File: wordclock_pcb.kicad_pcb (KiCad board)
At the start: 2 copper layers, 97.5 x 78.2 mm, 45 parts, among them IC1 ATmega328P, J1 MYUSBCONN5, J2 Stecker 1, J3 Stecker 2, J4 Stecker 3, Q1 2N3904, Q2 2N3904, SW1 MYSWITCH2, SW2 MYSWITCH_reduced, SW3 MYSWITCH_reduced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

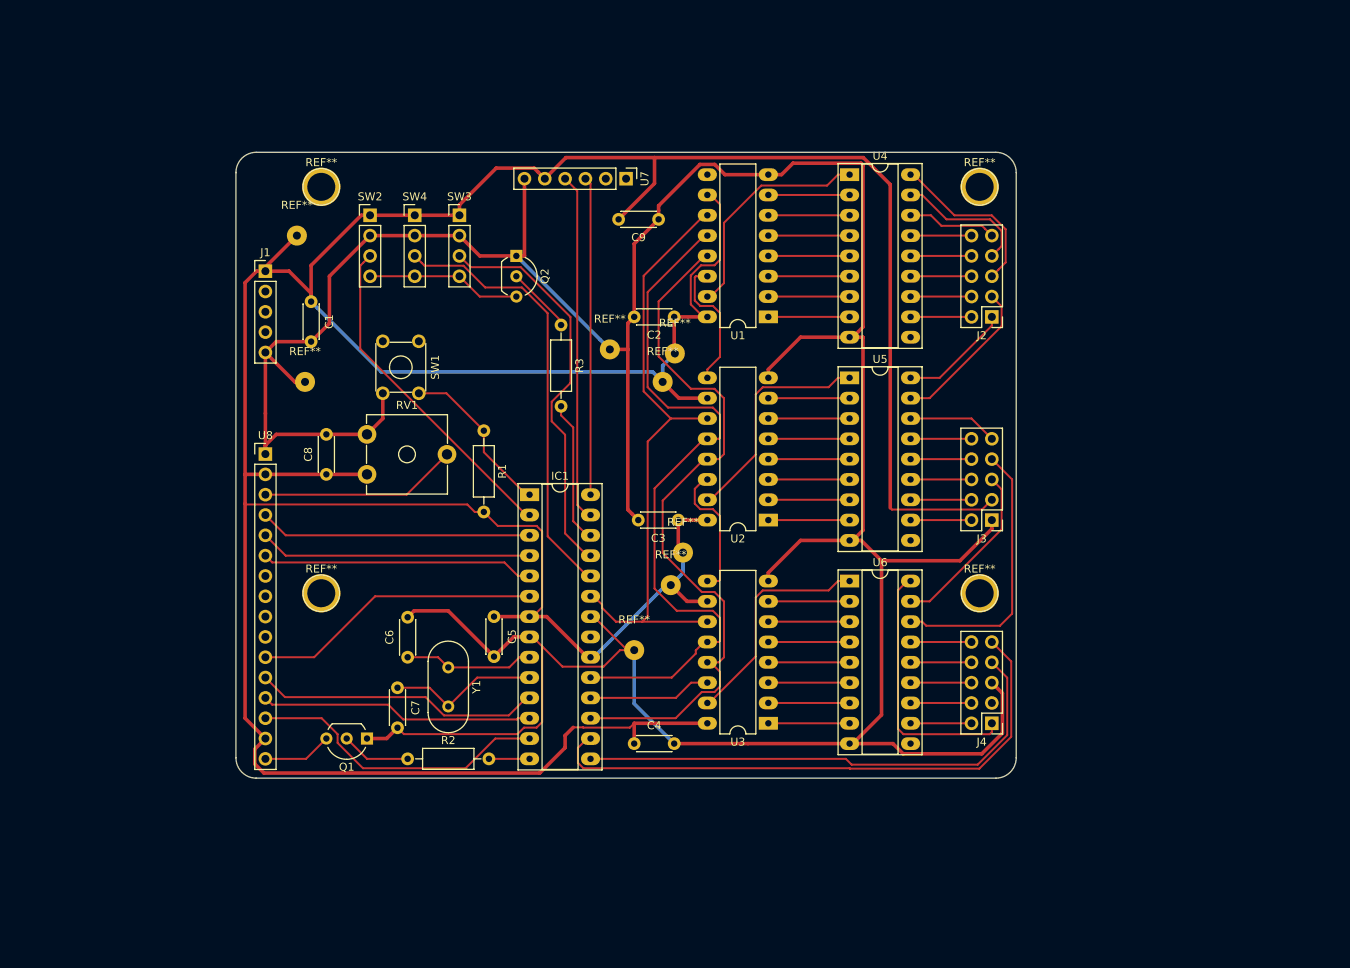
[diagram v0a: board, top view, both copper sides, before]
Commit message: Delete old pcb design and arrange footprints
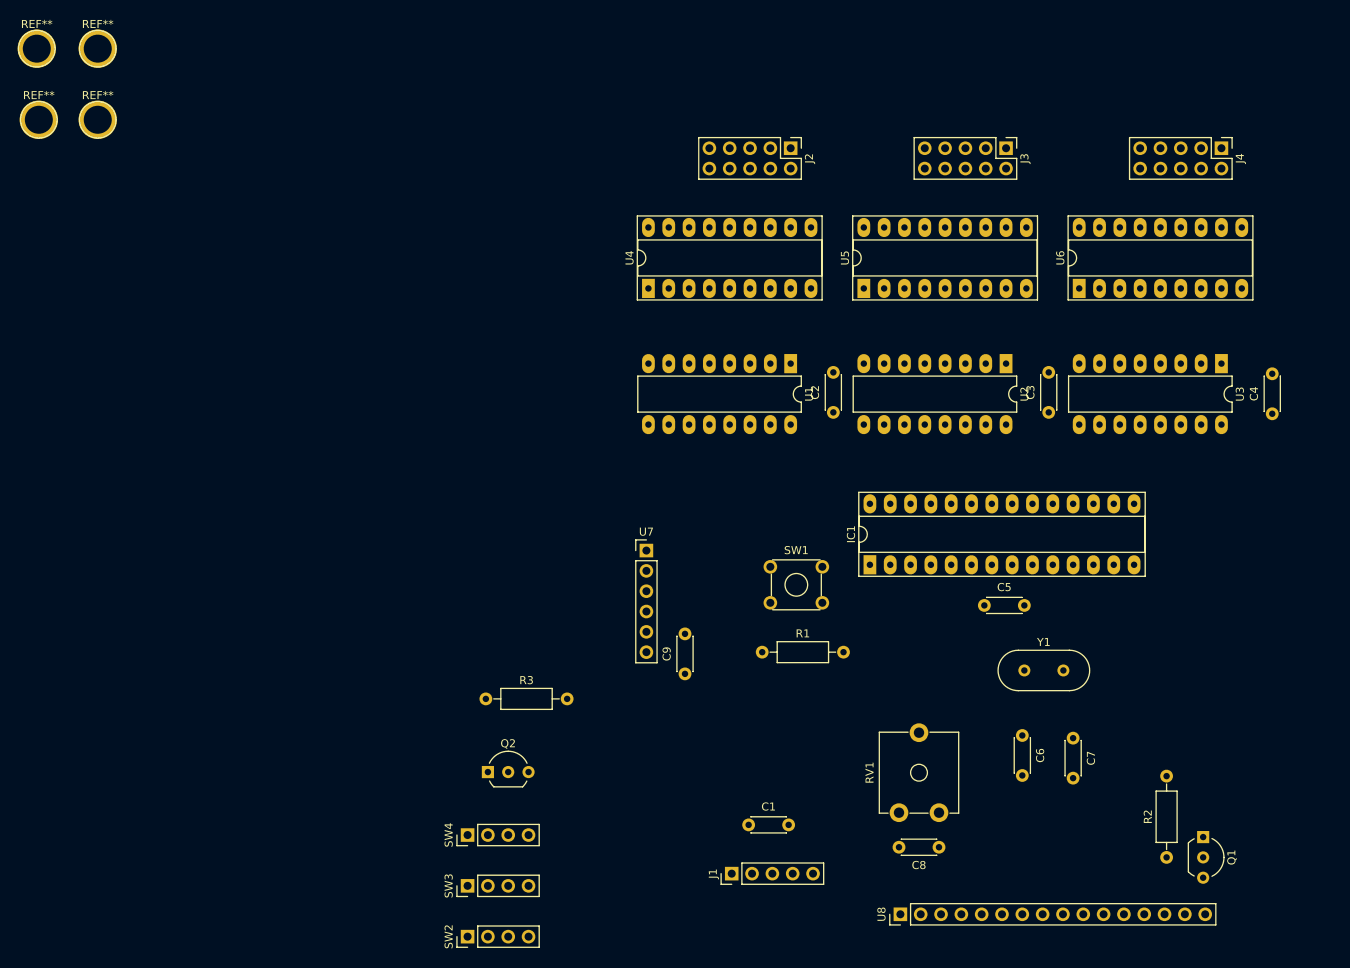
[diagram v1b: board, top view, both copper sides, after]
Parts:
- removed the REF** at (66.5, 79.2)
- removed the REF** at (113.8, 100.6)
- removed the REF** at (112.3, 104.6)
- removed the REF** at (104.6, 75.2)
- removed the REF** at (107.7, 112.8)
- removed the REF** at (65.5, 61.0)
- removed the REF** at (112.8, 75.7)
- removed the REF** at (111.3, 79.2)
- moved REF** 125.1 mm to (40.6, 46.5)
- moved REF** 111.6 mm to (40.6, 37.6)
- moved Q1 105.2 mm to (178.8, 136.1), turned to 270 degrees
- moved U8 98.0 mm to (141.0, 145.8), turned to 90 degrees
- moved R2 95.7 mm to (174.2, 138.7), turned to 90 degrees
- moved J1 95.2 mm to (119.9, 140.7), turned to 90 degrees
- moved SW2 91.0 mm to (86.9, 148.6), turned to 90 degrees
- moved C4 89.8 mm to (187.5, 83.2), turned to 90 degrees
- moved C8 89.6 mm to (145.8, 137.4), turned to 180 degrees
- moved C1 85.3 mm to (122.0, 134.6), turned to 0 degrees
- moved C7 84.7 mm to (162.6, 123.8)
- moved SW3 83.8 mm to (86.9, 142.2), turned to 90 degrees
- moved RV1 83.1 mm to (145.8, 133.1), turned to 90 degrees
- moved SW4 77.8 mm to (86.9, 135.9), turned to 90 degrees
- moved C6 77.5 mm to (156.2, 123.4), turned to 270 degrees
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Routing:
- net AVCC: track 489.6 -> 0.00 mm
- net GND: track 443.1 -> 0.00 mm
- net OE: track 92.1 -> 0.00 mm
- net STCP: track 91.1 -> 0.00 mm
- net SHCP: track 78.3 -> 0.00 mm
- net RGB_HAPPY: track 73.6 -> 0.00 mm
- net RGB_BIRTH: track 63.8 -> 0.00 mm
- net ENTER: track 55.3 -> 0.00 mm
- net DOWN: track 50.1 -> 0.00 mm
- net SDA: track 44.0 -> 0.00 mm
- net UP: track 42.7 -> 0.00 mm
- net SCL: track 40.2 -> 0.00 mm
- net D7: track 37.8 -> 0.00 mm
- net D4: track 36.2 -> 0.00 mm
- net D5: track 35.9 -> 0.00 mm
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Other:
- board outline removed

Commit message: First two layer version, needs refinement
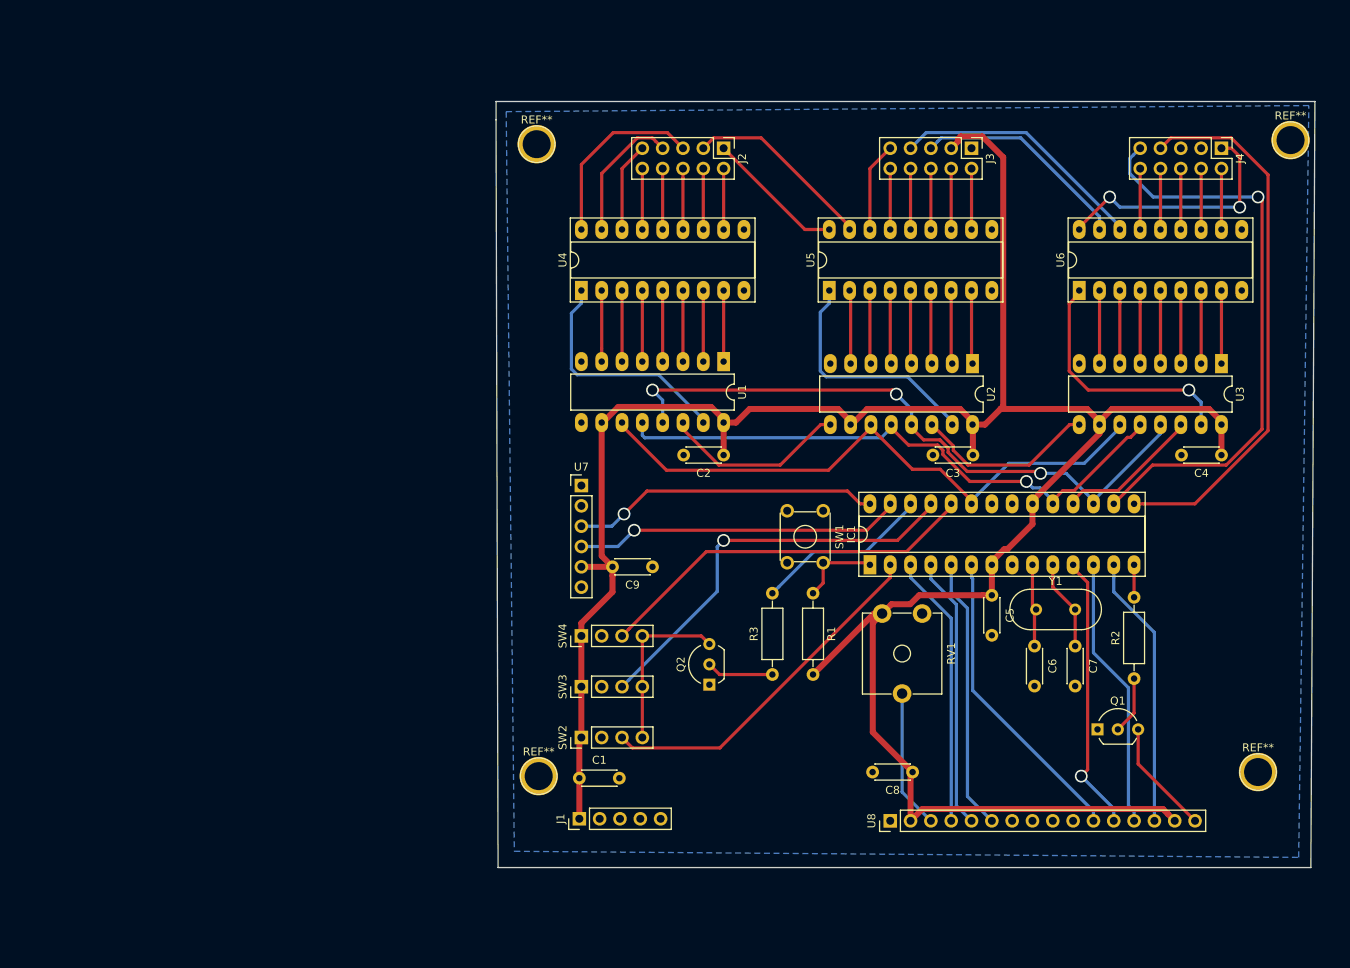
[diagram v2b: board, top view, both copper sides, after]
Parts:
- moved REF** 166.4 mm to (185.7, 128.0)
- moved REF** 149.5 mm to (189.7, 49.0)
- moved REF** 103.1 mm to (95.8, 128.5)
- moved REF** 63.6 mm to (95.5, 49.5)
- moved R3 35.9 mm to (125.0, 115.8), turned to 90 degrees
- moved Q2 29.8 mm to (117.1, 117.1), turned to 90 degrees
- moved SW2 28.7 mm to (101.1, 123.7)
- moved SW3 28.7 mm to (101.1, 117.3)
- moved SW4 28.7 mm to (101.1, 111.0)
- moved RV1 25.9 mm to (138.7, 108.2), turned to 270 degrees
- moved R2 22.7 mm to (170.2, 116.3)
- moved C1 22.0 mm to (100.8, 128.8)
- moved J1 20.2 mm to (100.8, 133.9)
- moved Q1 18.9 mm to (165.6, 122.7), turned to 0 degrees
- moved C2 14.7 mm to (118.9, 88.4), turned to 180 degrees
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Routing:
- net AVCC: track 0.00 -> 310.2 mm
- net OE: track 0.00 -> 80.5 mm, vias 0 -> 3
- net SHCP: track 0.00 -> 76.3 mm
- net STCP: track 0.00 -> 74.3 mm, vias 0 -> 1
- net RGB_HAPPY: track 0.00 -> 72.6 mm, vias 0 -> 1
- net RGB_BIRTH: track 0.00 -> 68.4 mm
- net DOWN: track 0.00 -> 51.6 mm, vias 0 -> 1
- net ENTER: track 0.00 -> 48.2 mm
- net UP: track 0.00 -> 44.5 mm
- net SDA: track 0.00 -> 41.1 mm, vias 0 -> 1
- net SCL: track 0.00 -> 38.6 mm, vias 0 -> 1
- net D4: track 0.00 -> 38.3 mm
- net D5: track 0.00 -> 34.8 mm, vias 0 -> 1
- net RW: track 0.00 -> 34.1 mm
- net E: track 0.00 -> 34.1 mm
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- added copper zone on B.Cu, net GND
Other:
- board outline added: 102.4 x 95.8 mm
- net class Default: trace_width 0.25 -> 0.4
- net class Power: trace_width 0.45 -> 0.75

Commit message: Change button order, tidy up some traces
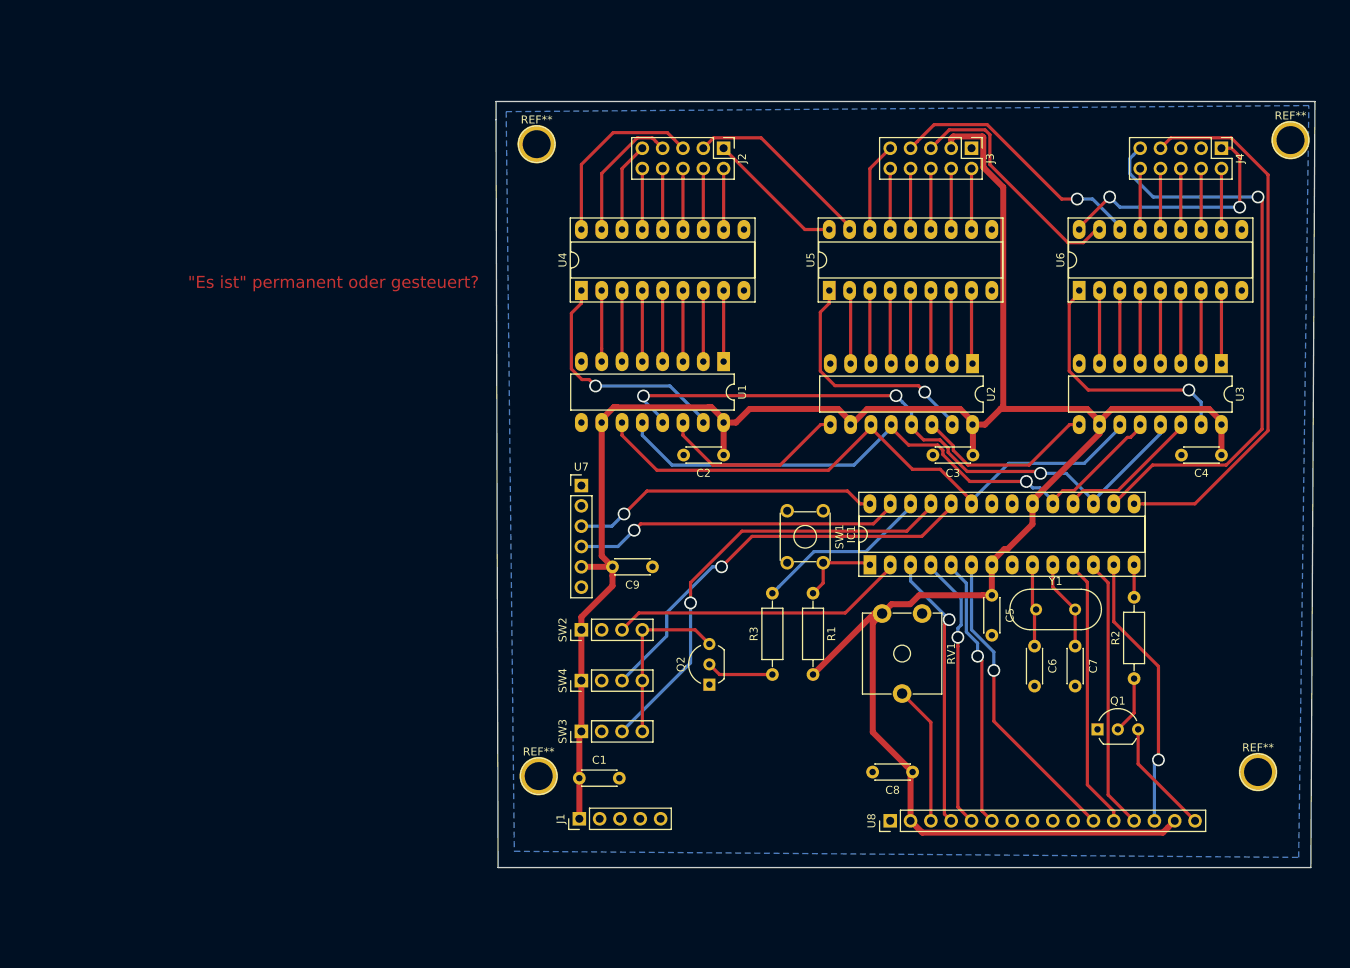
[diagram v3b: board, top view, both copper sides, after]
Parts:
- moved SW2 13.5 mm to (101.1, 110.2)
- moved SW3 5.59 mm to (101.1, 122.9)
- moved SW4 5.59 mm to (101.1, 116.6)
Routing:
- net UP: track 44.5 -> 37.1 mm
- net DOWN: track 51.6 -> 56.5 mm
- net ENTER: track 48.2 -> 52.2 mm, vias 0 -> 1
- net NEUN: track 27.3 -> 30.8 mm
- net STCP: track 74.3 -> 77.2 mm
- net ZEHN2: track 32.2 -> 33.0 mm, vias 0 -> 1
- net AVCC: track 310.2 -> 311.0 mm
- net SHCP: track 76.3 -> 77.0 mm
- net D5: track 34.8 -> 34.1 mm, vias 1 -> 0
- net RS: track 34.1 -> 34.6 mm, vias 0 -> 1
- net D7: track 34.1 -> 34.5 mm, vias 0 -> 1
- net RW: track 34.1 -> 34.4 mm, vias 0 -> 1
- net Net-(U2-Pad15): track 30.0 -> 30.2 mm, vias 0 -> 1
- net Net-(U1-Pad15): vias 0 -> 1
- net E: vias 0 -> 1
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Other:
- board text added: ""Es ist" permanent oder gesteuert?"
- board text added: "Abstand LED-Connector checken"
- board text added: "Bohrlöcher vertikalen Abstand an LED-Reihen anpassen"
- board text removed: "Leiterbahnen dicker"

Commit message: Add labeling to silkscreen, fix incorrect courtyard of SW1
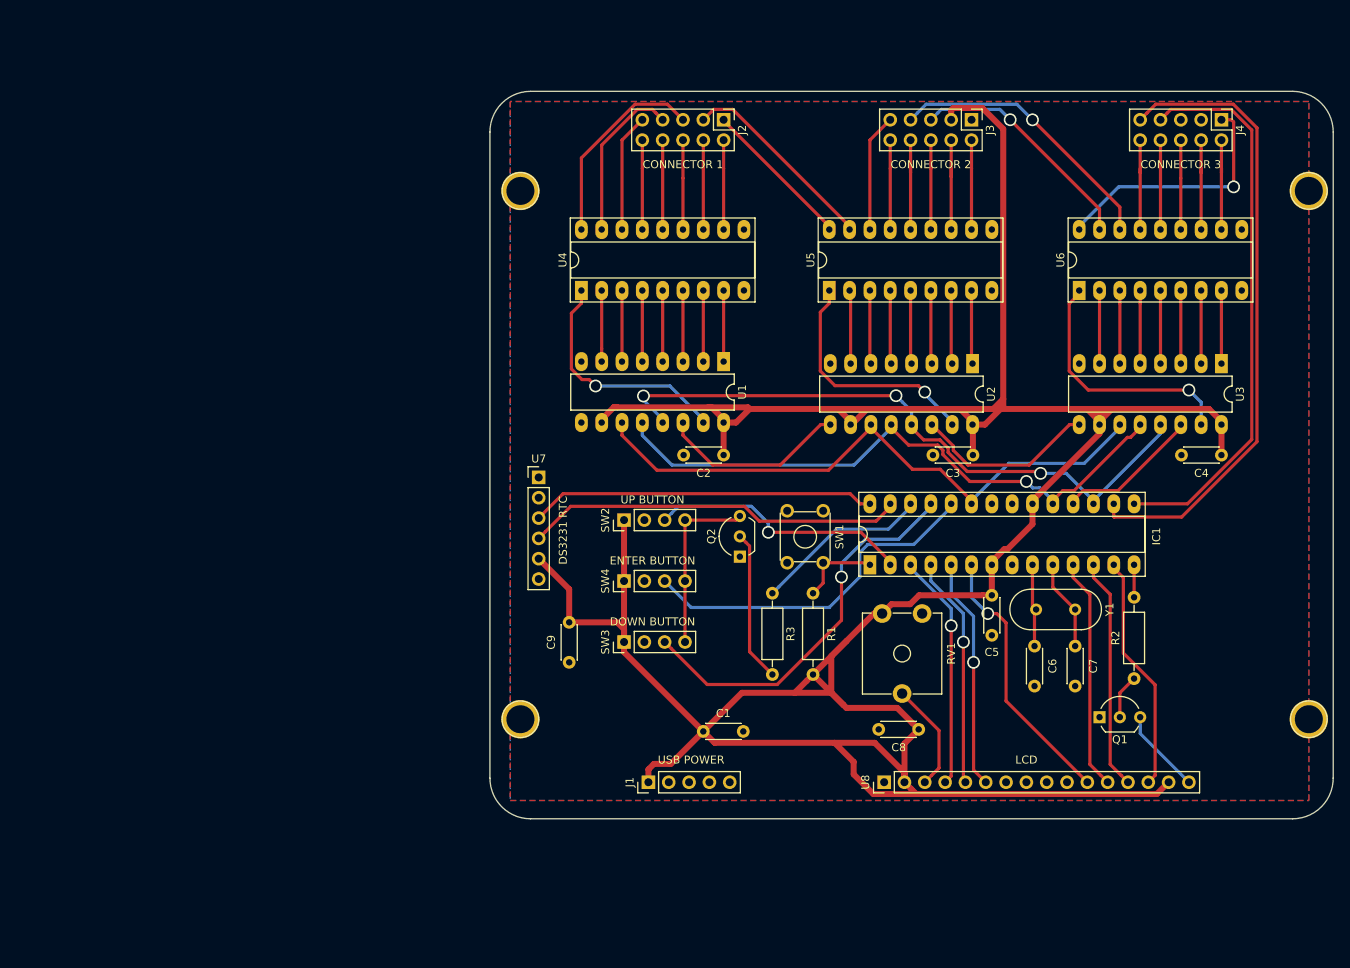
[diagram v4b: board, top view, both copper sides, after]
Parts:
- removed REF**: 1pin, Connectors:1pin
- added ?: 1pin, Connectors:1pin, F.Cu at (93.5, 55.4)
- SW1: footprint Buttons_Switches_THT:SW_TH_Tactile_Omron_B3F-10xx -> Button_Switch_THT:SW_TH_Tactile_Omron_B3F-10xx
- moved ? 96.7 mm to (192.0, 55.4)
- moved ? 96.5 mm to (192.0, 121.4)
- moved ? 92.4 mm to (93.5, 121.4)
- moved C1 16.6 mm to (116.3, 122.9)
- moved Q2 16.4 mm to (120.9, 101.1)
- moved C9 15.8 mm to (99.6, 114.3), turned to 90 degrees
- moved SW2 14.7 mm to (106.4, 96.5)
- moved SW4 13.5 mm to (106.4, 104.1)
- moved SW3 12.4 mm to (106.4, 111.8)
- moved J1 9.77 mm to (109.5, 129.3)
- moved U7 5.43 mm to (95.8, 91.2)
- moved C8 5.39 mm to (143.3, 122.7)
- moved U8 4.89 mm to (138.9, 129.3)
- moved J2 3.56 mm to (118.9, 46.5)
- moved J3 3.56 mm to (149.9, 46.5)
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- renumbered REF** to ?
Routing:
- net AVCC: track 311.0 -> 411.2 mm
- net Net-(Q2-Pad2): track 8.40 -> 19.0 mm
- net ENTER: track 52.2 -> 44.6 mm, vias 1 -> 0
- net DOWN: track 56.5 -> 49.2 mm
- net RGB_HAPPY: track 72.6 -> 79.3 mm, vias 1 -> 0
- net SDA: track 41.1 -> 47.5 mm, vias 1 -> 0
- net RW: track 34.4 -> 29.0 mm
- net E: track 34.1 -> 29.0 mm
- net D6: track 34.1 -> 29.0 mm
- net D5: track 34.1 -> 29.0 mm
- net RS: track 34.6 -> 29.6 mm
- net D7: track 34.5 -> 29.7 mm, vias 1 -> 0
- net SCL: track 38.6 -> 43.2 mm, vias 1 -> 0
- net VIERTEL: track 7.62 -> 12.2 mm
- net D4: track 38.3 -> 33.8 mm
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- added copper zone on F.Cu, net GND
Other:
- board size 102.4 x 95.8 mm -> 105.4 x 90.9 mm
- board text added: "CONNECTOR 1"
- board text added: "CONNECTOR 2"
- board text added: "CONNECTOR 3"
- board text added: "DOWN BUTTON"
- board text added: "DS3231 RTC"
- board text added: "ENTER BUTTON"
- board text added: "LCD"
- board text added: "UP BUTTON"
- board text added: "USB POWER"
- board text removed: ""Es ist" permanent oder gesteuert?"
- board text removed: "Abstand LED-Connector checken"
- board text removed: "Bohrlöcher vertikalen Abstand an LED-Reihen anpassen"
- board text removed: "mehr Anschlüsse"

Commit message: Add description
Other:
- board text added: "Wordclock control board v1.1"
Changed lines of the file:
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@@
   (general
     (thickness 1.6)
-    (drawings 17)
+    (drawings 18)
     (tracks 464)
     (zones 0)
@@
     (pad 1 thru_hole circle (at 0 0) (size 4.8 4.8) (drill 3.5) (layers *.Cu *.Mask))
   )
+  (gr_text "Wordclock control board v1.1" (at 191.516 89.154 90) (layer F.SilkS)
+    (effects (font (size 2 2) (thickness 0.15)))
+  )
   (gr_text LCD (at 156.718 126.492) (layer F.SilkS)
